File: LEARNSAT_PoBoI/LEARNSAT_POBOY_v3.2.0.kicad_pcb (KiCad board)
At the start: 4 copper layers, 90.2 x 95.8 mm, 471 parts, among them J1 FTSH-105-01-L-DV-K-P-TR, J5 FTSH-105-01-L-DV-K-P-TR, P1 22-28-4036, Q1 SI7164DP-T1-GE3, Q10 SI5418DU-T1-GE3, Q11 SI7164DP-T1-GE3, Q12 SI5418DU-T1-GE3, Q13 SI5418DU-T1-GE3, Q13 SI7164DP-T1-GE3, Q14 SI5418DU-T1-GE3, Q14 SI7164DP-T1-GE3, Q15 SI7164DP-T1-GE3, Q16 SI5418DU-T1-GE3, Q17 SI7164DP-T1-GE3, Q18 SI5418DU-T1-GE3, Q19 SI7164DP-T1-GE3, Q2 SI7164DP-T1-GE3, Q20 SI5418DU-T1-GE3, Q20 SI7164DP-T1-GE3, Q21 SI7164DP-T1-GE3, Q22 SI5418DU-T1-GE3, Q23 SI7164DP-T1-GE3, Q24 SI5418DU-T1-GE3, Q3 SI7164DP-T1-GE3, Q4 SI5418DU-T1-GE3, Q5 SI5418DU-T1-GE3, Q6 SI7164DP-T1-GE3, Q7 SI7164DP-T1-GE3, Q8 SI5418DU-T1-GE3, Q9 SI5418DU-T1-GE3, SW1 B3U-1000P, SW2 B3U-1000P, SW3 TS04-66-43-BK-100-SMT, U1 MAX6746KA29+T, U1 STM32F103RET6, U10 LM2622MMX-ADJ/NOPB, U11 LM2622MMX-ADJ/NOPB, U12 INA219AIDCNR, U13 INA219AIDCNR, U14 INA219AIDCNR, U15 LTC4231IUD-2#TRPBF, U16 LTC4231IUD-2#TRPBF, U17 LP5907SNX-3.3, U18 LP5907SNX-3.3, U18 LTC4231IUD-2#TRPBF, U19 INA219AIDCNR, U2 SN74AUP1G08QDCKRQ1, U20 INA219AIDCNR, U21 74AC14MTCX, U22 LTC4231IUD-2#TRPBF, U22 LTC4304CMS#PBF, U23 INA219AIDCNR, U23 SN74LVC1G373DCKR, U24 LTC4231IUD-2#TRPBF, U25 INA219AIDCNR, U25 LTC4231IUD-2#TRPBF, U26 ISL3259EIRZ, U26 LTC4231IUD-2#TRPBF, U27 INA219AIDCNR, U28 LTC4231IUD-2#TRPBF, U29 INA219AIDCNR, U29 LTC4231IUD-2#TRPBF, U3 MAX6746KA29+T, U30 INA219AIDCNR, U30 LTC4231IUD-2#TRPBF, U31 INA219AIDCNR, U32 LTC4231IUD-2#TRPBF, U33 INA219AIDCNR, U34 MAX6746KA29+T, U35 MAX6746KA29+T, U36 SN74AUP1G08QDCKRQ1, U37 SN74AUP1G08QDCKRQ1, U38 LTC4304CMS#PBF, U39 74AC14MTCX, U4 SN74AUP1G08QDCKRQ1, U40 SN74LVC1G373DCKR, U41 ISL3259EIRZ, U5 LT1616ES6#TRMPBF, U50 LM2622MMX-ADJ/NOPB, U51 LM2622MMX-ADJ/NOPB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

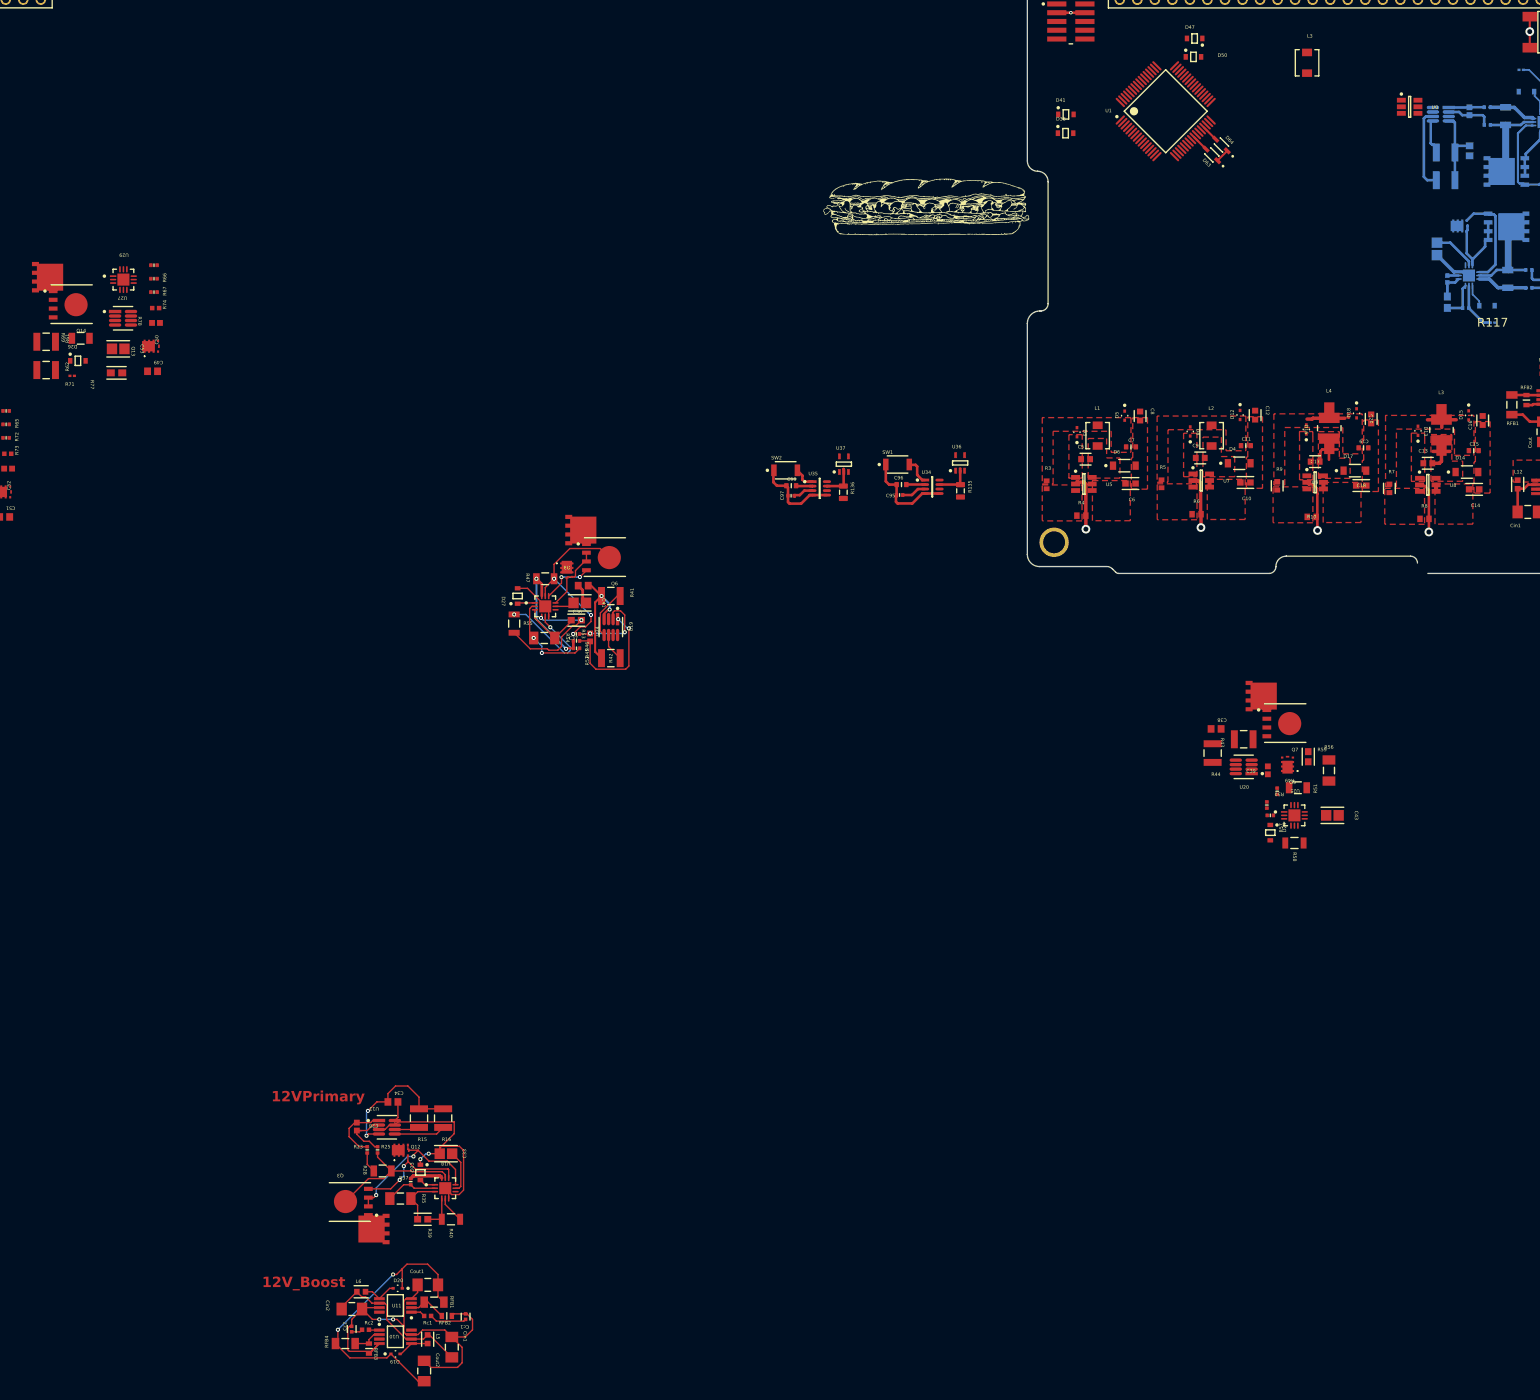
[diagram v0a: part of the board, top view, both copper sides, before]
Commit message: Edited 12V Rail schematics
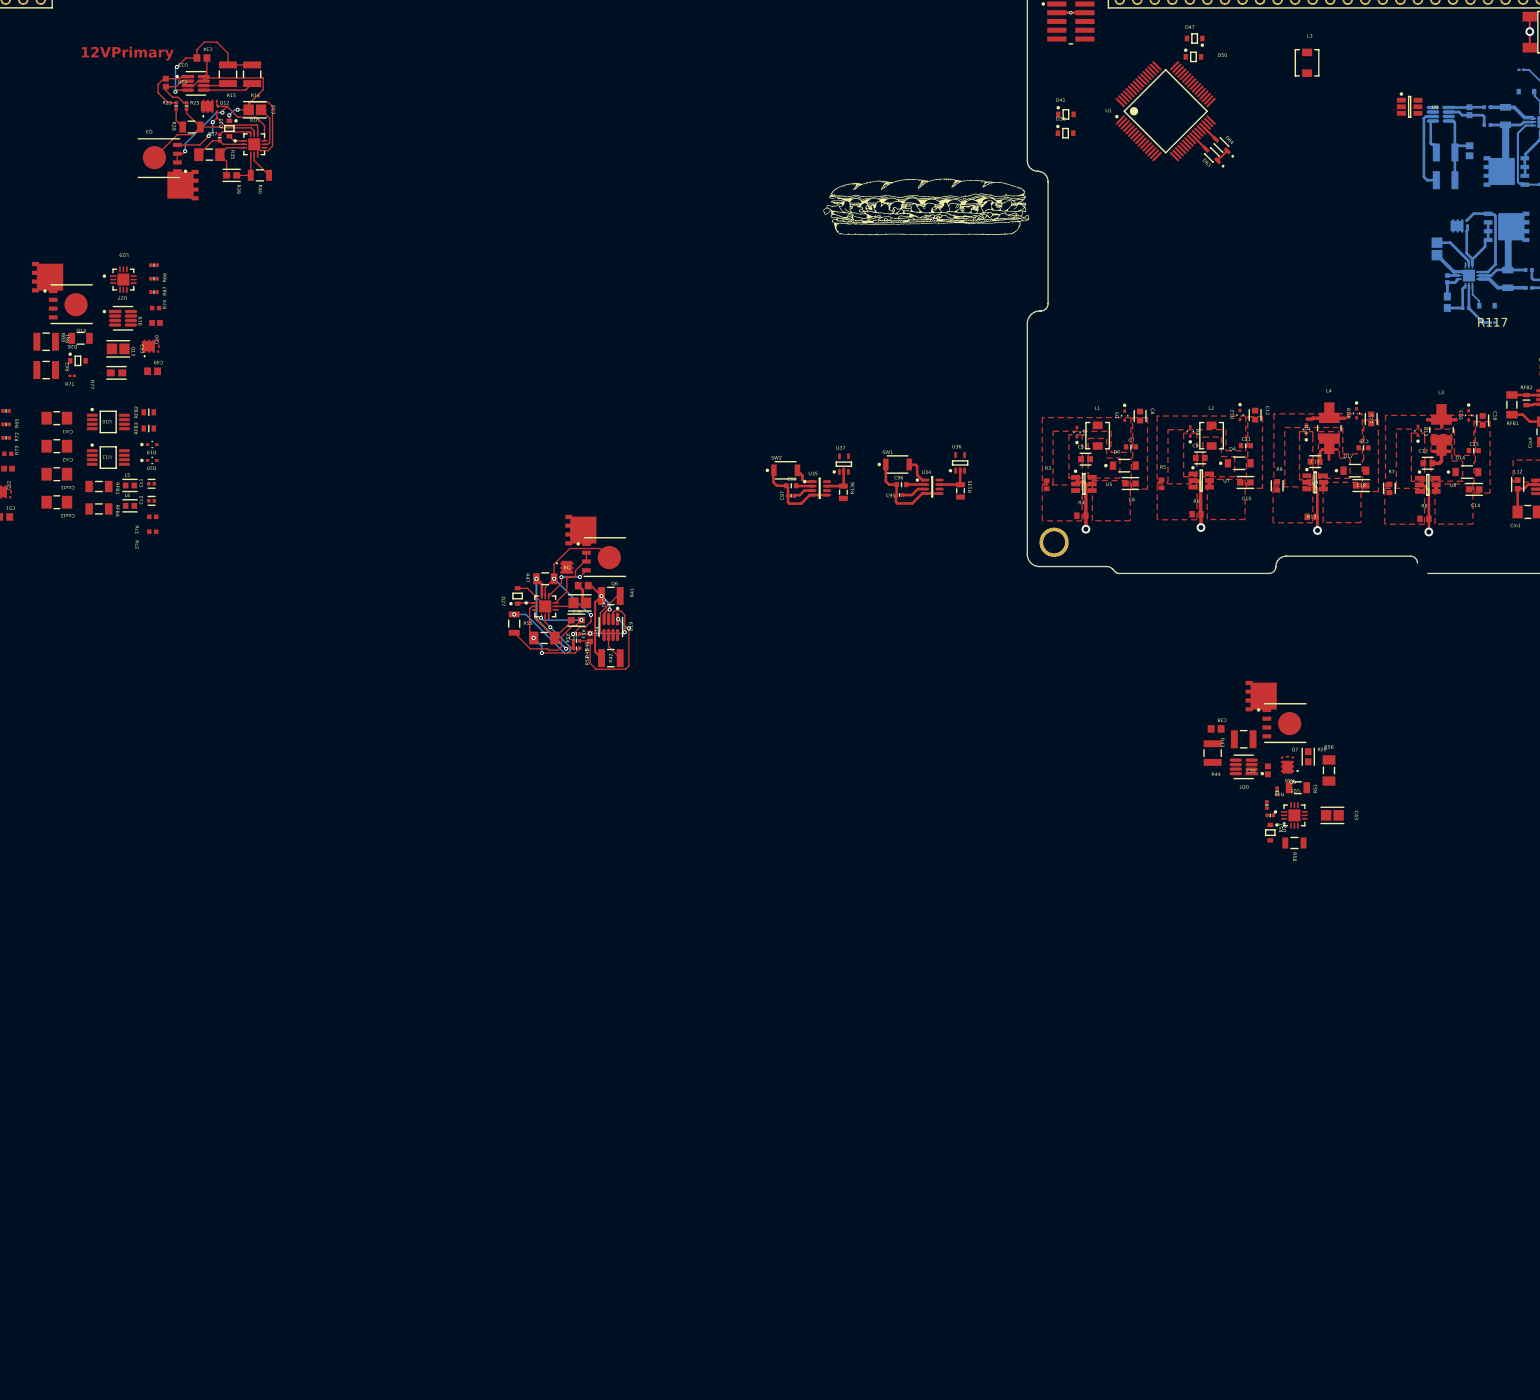
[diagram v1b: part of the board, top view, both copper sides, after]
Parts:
- moved C28 153.7 mm to (207.3, 79.0)
- moved C33 153.7 mm to (220.2, 82.9)
- moved C34 153.7 mm to (212.5, 75.4)
- moved D23 153.7 mm to (216.5, 85.6)
- moved Q12 153.7 mm to (213.5, 82.5)
- moved Q3 153.7 mm to (206.3, 89.9)
- moved R15 153.7 mm to (216.3, 77.7)
- moved R16 153.7 mm to (219.8, 77.7)
- moved R23 153.7 mm to (208.8, 82.3)
- moved R25 153.7 mm to (210.3, 82.3)
- moved R28 153.7 mm to (211.0, 85.4)
- moved R35 153.7 mm to (213.6, 89.4)
- moved R37 153.7 mm to (215.1, 86.9)
- moved R40 153.7 mm to (221.0, 92.4)
- moved U13 153.7 mm to (211.7, 79.1)
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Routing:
- net GND: track 272.3 -> 213.6 mm, vias 19 -> 17
- net ???: track 44.4 -> 0.00 mm, vias 2 -> 0
- net VBatt Primary: track 22.8 -> 0.00 mm
- net Net-(U11-FB): track 5.56 -> 0.00 mm
- net Net-(Cc1-Pad1): track 5.41 -> 0.00 mm
- net Net-(D20-A): track 5.04 -> 0.00 mm
- net Net-(D19-A): track 4.62 -> 0.00 mm
- net Net-(U10-FB): track 4.38 -> 0.00 mm
- net Net-(U11-VC): track 2.08 -> 0.00 mm
- net Net-(Cc2-Pad1): track 1.62 -> 0.00 mm
- net Net-(U10-VC): track 1.52 -> 0.00 mm
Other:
- board text removed: "12V_Boost"
